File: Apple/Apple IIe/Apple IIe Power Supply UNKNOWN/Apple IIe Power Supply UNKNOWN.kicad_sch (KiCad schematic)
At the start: 35 parts, among them P21 Conn_01x03, Q1 OSC, Q2 DRIVER, T1 Transformer_1P_1S, T3 Transformer_1P_2S_IIe_PS

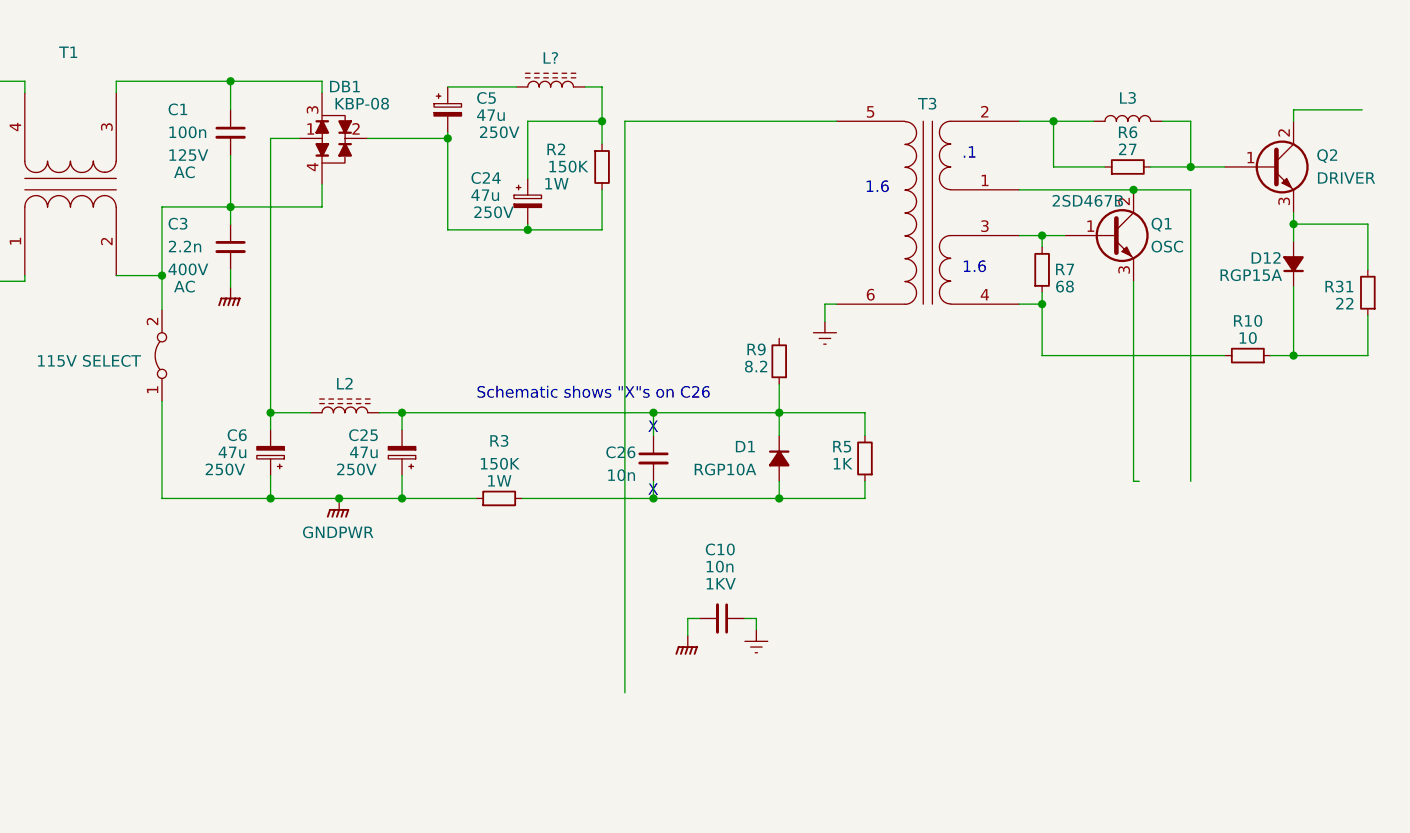
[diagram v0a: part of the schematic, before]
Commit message: Pausing on the T18231 IC (and big Transformer)
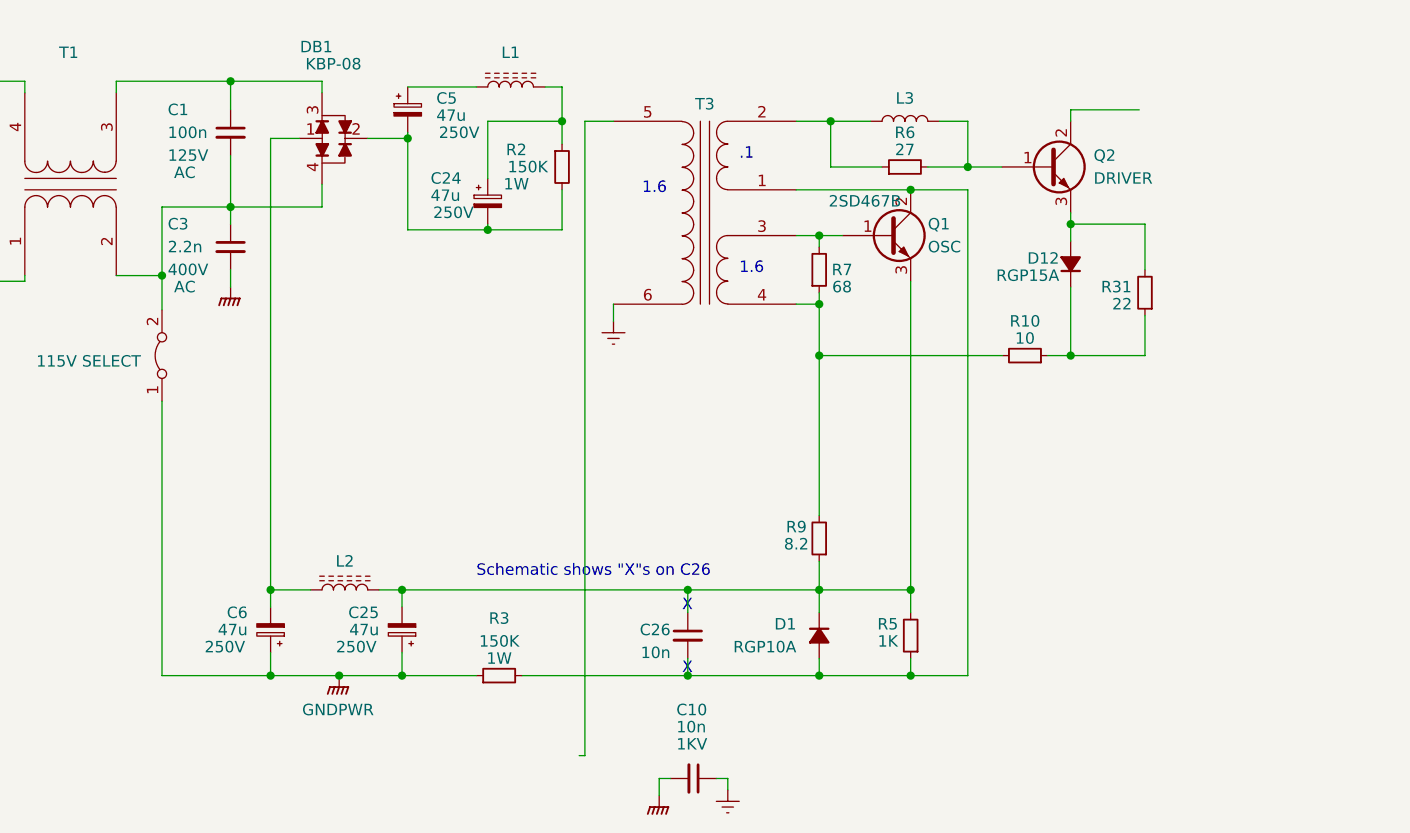
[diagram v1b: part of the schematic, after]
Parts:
- gave numbers to parts that had none: 1
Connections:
- net at R10.2, R7.1, T3.4 (SD): now also R9.2
- net at Q1.2 (C), T3.1 (SB): now also C26.2, D1.2 (A), R3.2, R5.1
- net at C25.2, C26.1, D1.1 (K)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: now also Q1.3 (E)
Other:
- moved on the sheet: C10, C24, C25, C26, C5, C6, D1, D12, L1, L2, L3, Q1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

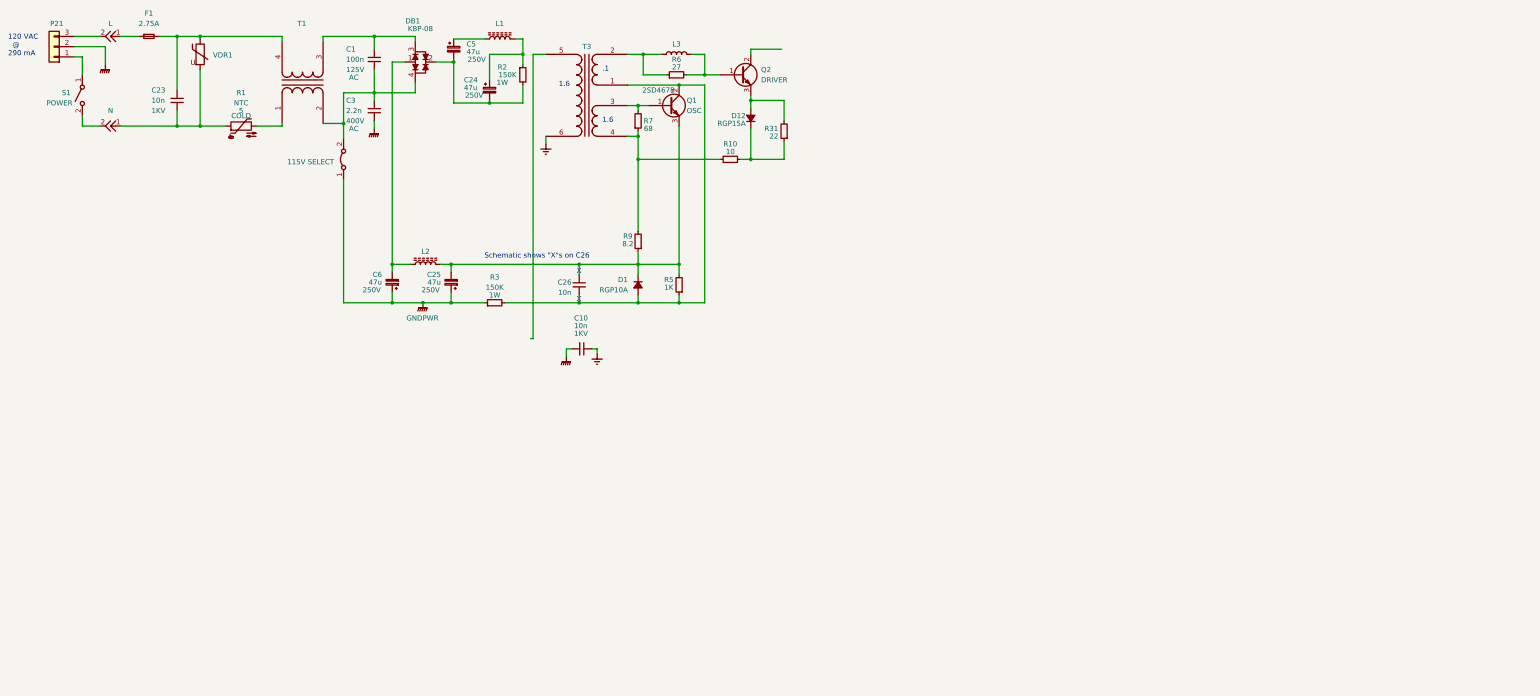
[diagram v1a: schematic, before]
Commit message: Created T2 and drew in its connections.
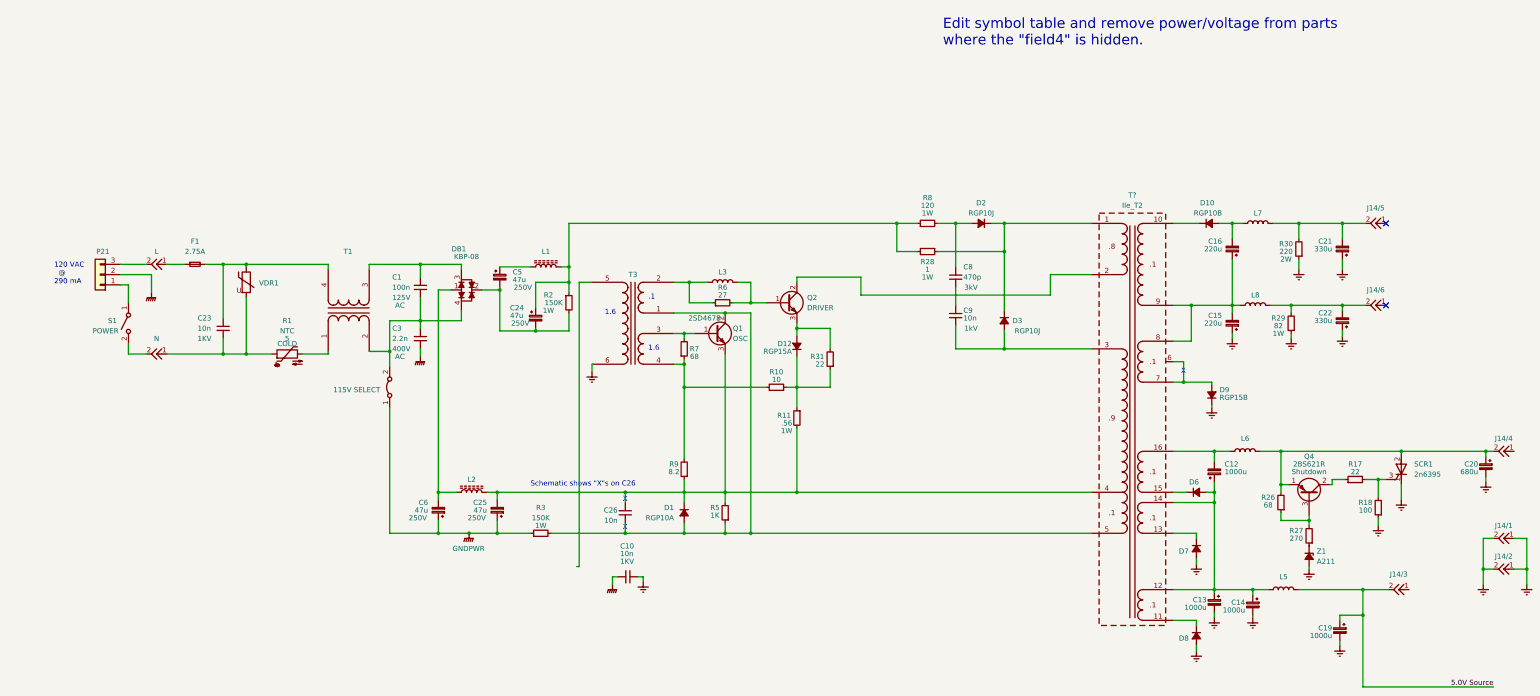
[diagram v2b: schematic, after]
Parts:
- added C12, C13, C14, C19: 1000u, symbol Device:C_Polarized_Small
- added C15, C16: 220u, symbol Device:C_Polarized_Small
- added C20: 680u, symbol Device:C_Polarized_Small
- added C21, C22: 330u, symbol Device:C_Polarized_Small
- added C8: 470p, symbol Device:C_Small
- added C9: 10n, symbol Device:C_Small
- added D10: RGP10B, symbol Device:D_Small_Filled
- added D2, D3: RGP10J, symbol Device:D_Small_Filled
- added D6, D7, D8, D9: RGP15B, symbol Device:D_Small_Filled
- added J14/1, J14/2, J14/3, J14/4, J14/5, J14/6: Conn_Off_Board, symbol Apple IIe Power Supply UNKNOWN Library:Conn_Off_Board
- added L5, L6, L7, L8: L, symbol Device:L
- added Q4: 2BS621R, symbol Device:Q_PNP_ECB
- added R11: .56, symbol Device:R_Small
- added R17: 22, symbol Device:R_Small
- added R18: 100, symbol Device:R_Small
- added R26: 68, symbol Device:R_Small
- added R27: 270, symbol Device:R_Small
- added R28: 1, symbol Device:R_Small
- added R29: 82, symbol Device:R_Small
- added R30: 220, symbol Device:R_Small
- added R8: 120, symbol Device:R_Small
- added SCR1: 2n6395, symbol Device:Q_SCR_KAG
- added T?: IIe_T2, symbol Apple IIe Power Supply UNKNOWN Library:IIe_T2
- added Z1: A211, symbol Device:D_Zener_Small_Filled
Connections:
- net Earth: now also C13.2, C14.2, C15.1, C19.2, C20.2, C21.1, C22.1, D7.2 (A), D8.2 (A), D9.1 (K), J14/1.1, J14/1.2, J14/2.1, J14/2.2, R18.1, R29.1, R30.1, SCR1.1 (K), Z1.2 (A)
- net at C26.2, D1.2 (A), Q1.2 (C)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: now also T?.5 (AB)
- net at C25.2, C26.1, D1.1 (K)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: now also R11.2, T?.4 (AA)
- net at C24.1, L1.2, R2.1: now also R28.2, R8.1
- net at D12.1 (K), R10.1, R31.1: now also R11.1
- net at Q2.2 (C): now also T?.2 (AA)
- new net: C12.2, L6.1, T?.16 (SA)
- new net: C20.1, J14/4.2, L6.2, Q4.1 (E), R26.2, SCR1.2 (A)
- new net: C15.2, C16.1, L8.1, T?.8 (SA), T?.9 (SB)
- new net: C21.2, J14/5.2, L7.2, R30.2
- new net: C12.1, C13.1, C14.1, D6.2 (A), L5.1, T?.12 (SC), T?.14 (SC)
- new net: D2.1 (K), D3.1 (K), R28.1, T?.1 (AA)
- new net: D10.1 (K), T?.10 (SA)
- new net: D8.1 (K), T?.11 (SD)
- new net: D7.1 (K), T?.13 (SD)
- new net: D6.1 (K), T?.15 (SB)
- new net: C9.2, D3.2 (A), T?.3 (AA)
- new net: D9.2 (A), T?.6 (SB), T?.7 (SB)
- new net: C8.1, D2.2 (A), R8.2
- new net: C22.2, J14/6.2, L8.2, R29.2
- new net: C16.2, D10.2 (A), L7.1
- new net: Q4.2 (C), R17.1
- new net: R17.2, R18.2, SCR1.3 (G)
- new net: R27.1, Z1.1 (K)
- new net: Q4.3 (B), R26.1, R27.2
- new net: C8.2, C9.1
- new net 5.0V Source: C19.1, J14/3.2, L5.2
- no-connect marks 0 -> 2
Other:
- note added: "Edit symbol table and remove power/voltage from parts where the "field4" is hidden."
- moved on the sheet: C1, C10, C23, C24, C25, C26, C3, C5, C6, D1, D12, DB1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

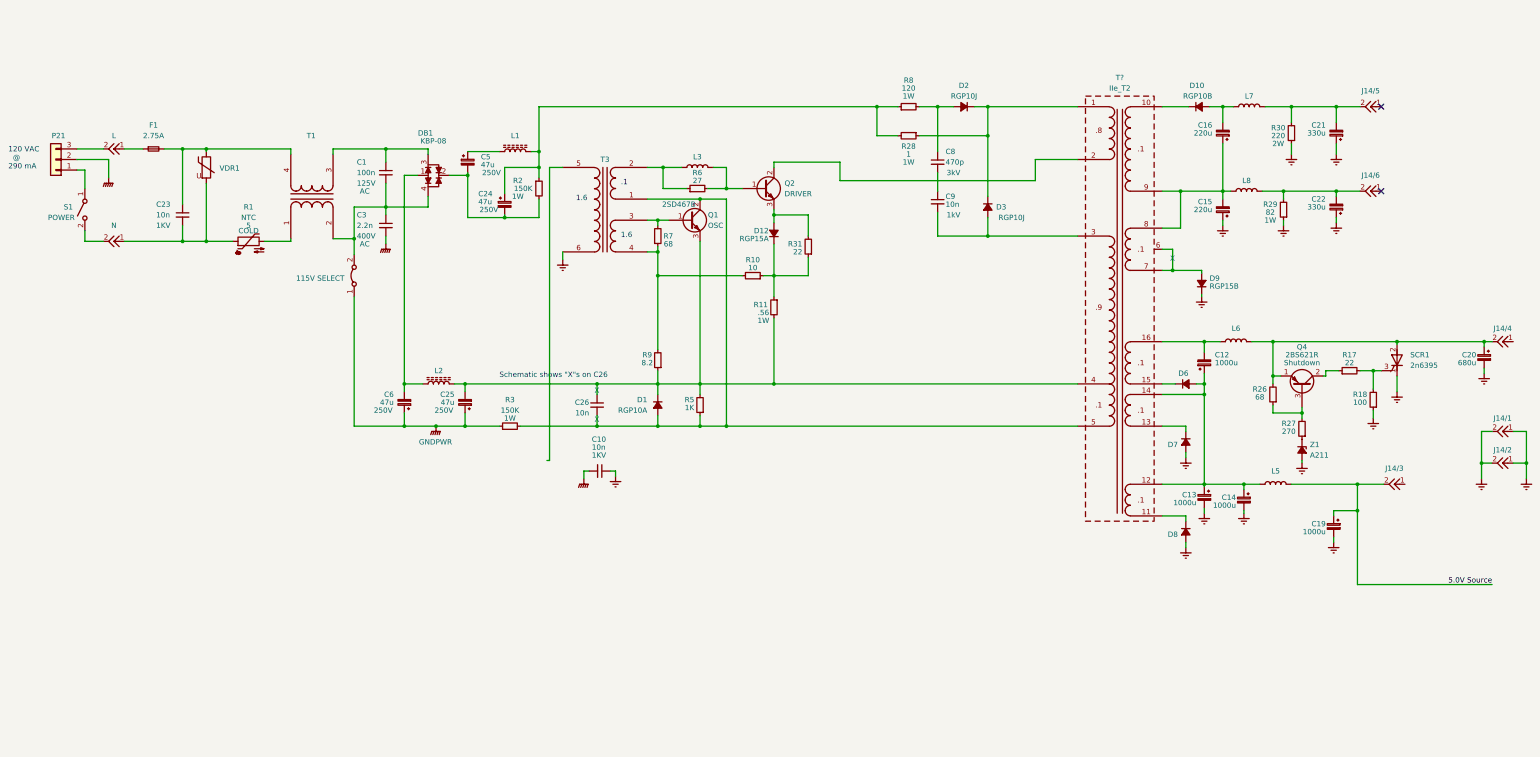
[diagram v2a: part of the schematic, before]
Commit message: finish the re-copy step. now doing erc.
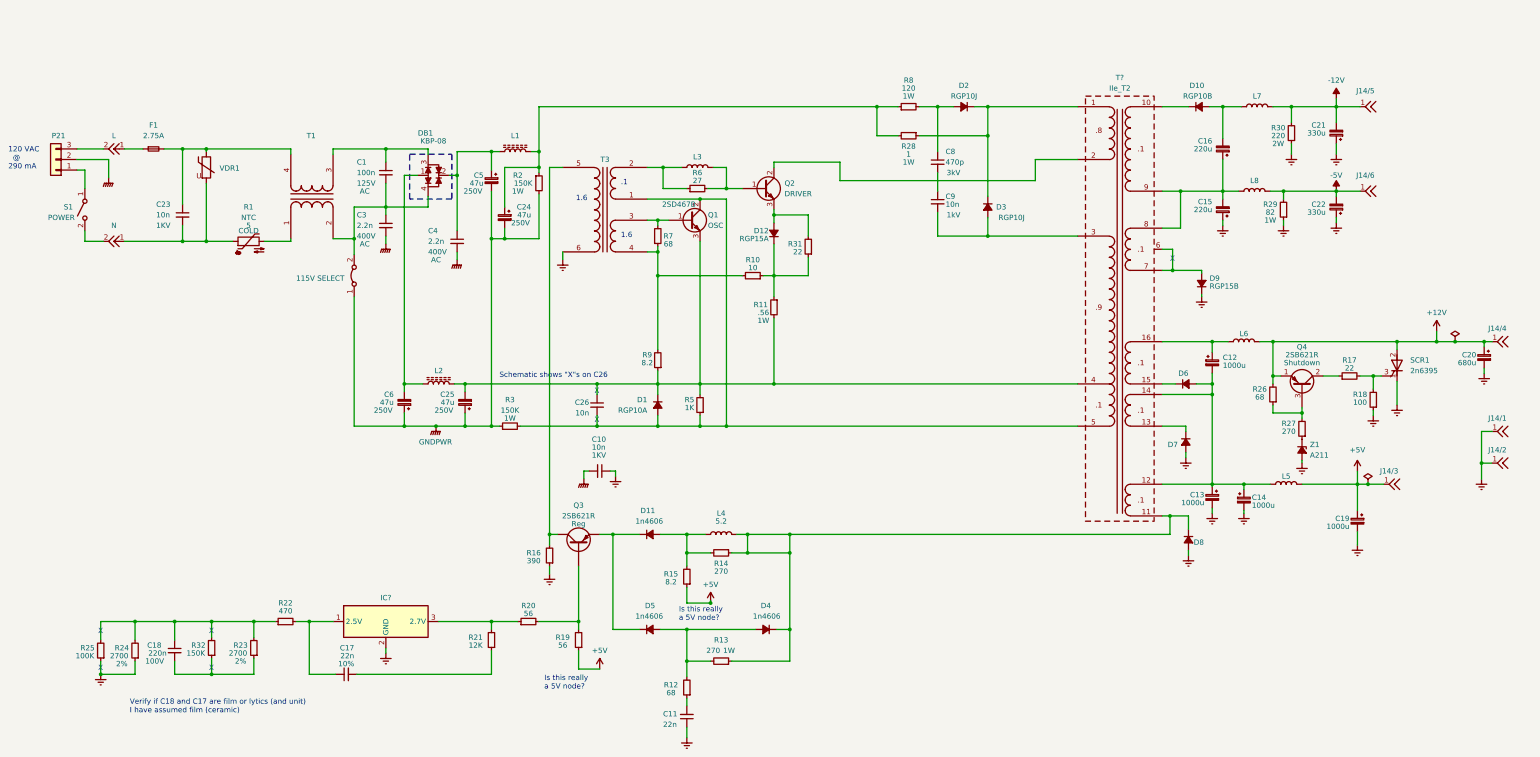
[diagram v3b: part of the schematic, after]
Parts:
- added C11, C17: 22n, symbol Device:C_Small
- added C18: 220n, symbol Device:C_Small
- added C4: 2.2n, symbol Device:C_Small
- added D11, D4, D5: 1n4606, symbol Device:D_Small_Filled
- added IC?: ~, symbol Apple IIe Power Supply UNKNOWN Library:T18231
- added L4: 5.2, symbol Device:L
- added Q3: 2SB621R, symbol Apple IIe Power Supply UNKNOWN Library:Q_PNP_NO_NUMBERS
- added R12: 68, symbol Device:R_Small
- added R13, R14: 270, symbol Device:R_Small
- added R15: 8.2, symbol Device:R_Small
- added R16: 390, symbol Device:R_Small
- added R19, R20: 56, symbol Device:R_Small
- added R21: 12K, symbol Device:R_Small
- added R22: 470, symbol Device:R_Small
- added R23, R24: 2700, symbol Device:R_Small
- added R25: 100K, symbol Device:R_Small
- added R32: 150K, symbol Device:R_Small
- J14/1, J14/2, J14/3, J14/4, J14/5, J14/6: symbol Apple IIe Power Supply UNKNOWN Library:Conn_Off_Board -> Apple IIe Power Supply UNKNOWN Library:Conn_Off_Board_Single
- Q4: value 2BS621R -> 2SB621R
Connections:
- net Earth: now also C11.1, IC?.2 (GND), R16.1, R24.1, R25.1; no longer J14/1.2, J14/2.2
- net GNDPWR: now also C24.2, C5.2, R2.2, C4.2
- net at L6.1, T?.16 (SA): now also C12.1; no longer C12.2
- net +12V: now reaches C20.1, L6.2, Q4.1 (E), R26.2, SCR1.2 (A)
- net +12V: now also J14/4.1; no longer J14/4.2
- net at C5.1, L1.1: now also DB1.2, C4.1
- net -12V: now reaches C21.2, L7.2, R30.2
- net -12V: now also J14/5.1; no longer J14/5.2
- net at T3.5 (AA): now also Q3. (E), R16.2
- net at C13.1, C14.1, D6.2 (A)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: now also C12.2; no longer C12.1
- net at D8.1 (K), T?.11 (SD): now also D4.1 (K), L4.2, R13.1, R14.1
- net -5V: now reaches C22.2, L8.2, R29.2
- net -5V: now also J14/6.1; no longer J14/6.2
- net +5V: now reaches J14/3.1
- net +5V: now also C19.1, L5.2, R15.1, R19.1
- removed net 5.0V Source: C19.1, J14/3.2, L5.2
- new net: C18.1, R22.1, R23.2, R24.2, R25.2, R32.2
- new net: C17.2, R21.1
- new net: IC?.3 (2.7V), R20.1, R21.2
- new net: C18.2, R23.1, R32.1
- new net: D4.2 (A), D5.2 (A), R12.2, R13.2
- new net: Q3. (E), R19.2, R20.2
- new net: D11.1 (K), D5.1 (K), Q3. (E)
- new net: C17.1, IC?.1 (2.5V), R22.2
- new net: D11.2 (A), L4.1, R14.2, R15.2
- new net: C11.2, R12.1
- no-connect marks 2 -> 0
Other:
- note added: "Is this really a 5V node?"
- note added: "Verify if C18 and C17 are film or lytics (and unit) I have assumed film (ceramic)"
- moved on the sheet: C12, C13, C16, C19, C24, C5, D8, L5, L6, L7, L8, R17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

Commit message: created v1 pdf
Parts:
- IC1: renamed from IC?; Field4 (none) -> REG
- gave numbers to parts that had none: 2
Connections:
- net at R7.2, T3.3 (SC): now also Q1. (E); no longer Q1.1 (B)
- net at C26.2, D1.2 (A), R3.2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: now also Q1. (E); no longer Q1.2 (C)
- net at C25.2, C26.1, D1.1 (K)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: now also Q1. (E); no longer Q1.3 (E)
- net at T2.2 (AA): now also Q2. (E); no longer Q2.2 (C)
- net at L3.2, R6.2: now also Q2. (E); no longer Q2.1 (B)
- net at D12.2 (A), R31.2: now also Q2. (E); no longer Q2.3 (E)
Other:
- moved on the sheet: C1, C10, C11, C12, C13, C14, C15, C16, C17, C18, C19, C20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
